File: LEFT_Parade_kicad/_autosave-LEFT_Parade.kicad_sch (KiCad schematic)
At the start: 31 parts, among them SW1 RotaryEncoder_Switch, SW10 SW_Push_reverse, SW11 SW_Push_reverse, SW12 SW_Push_reverse, SW13 SW_Push_reverse, SW14 SW_Push_reverse, SW15 SW_Push_reverse, SW16 SW_Push_reverse, SW17 SW_Push_reverse, SW2 SW_Push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

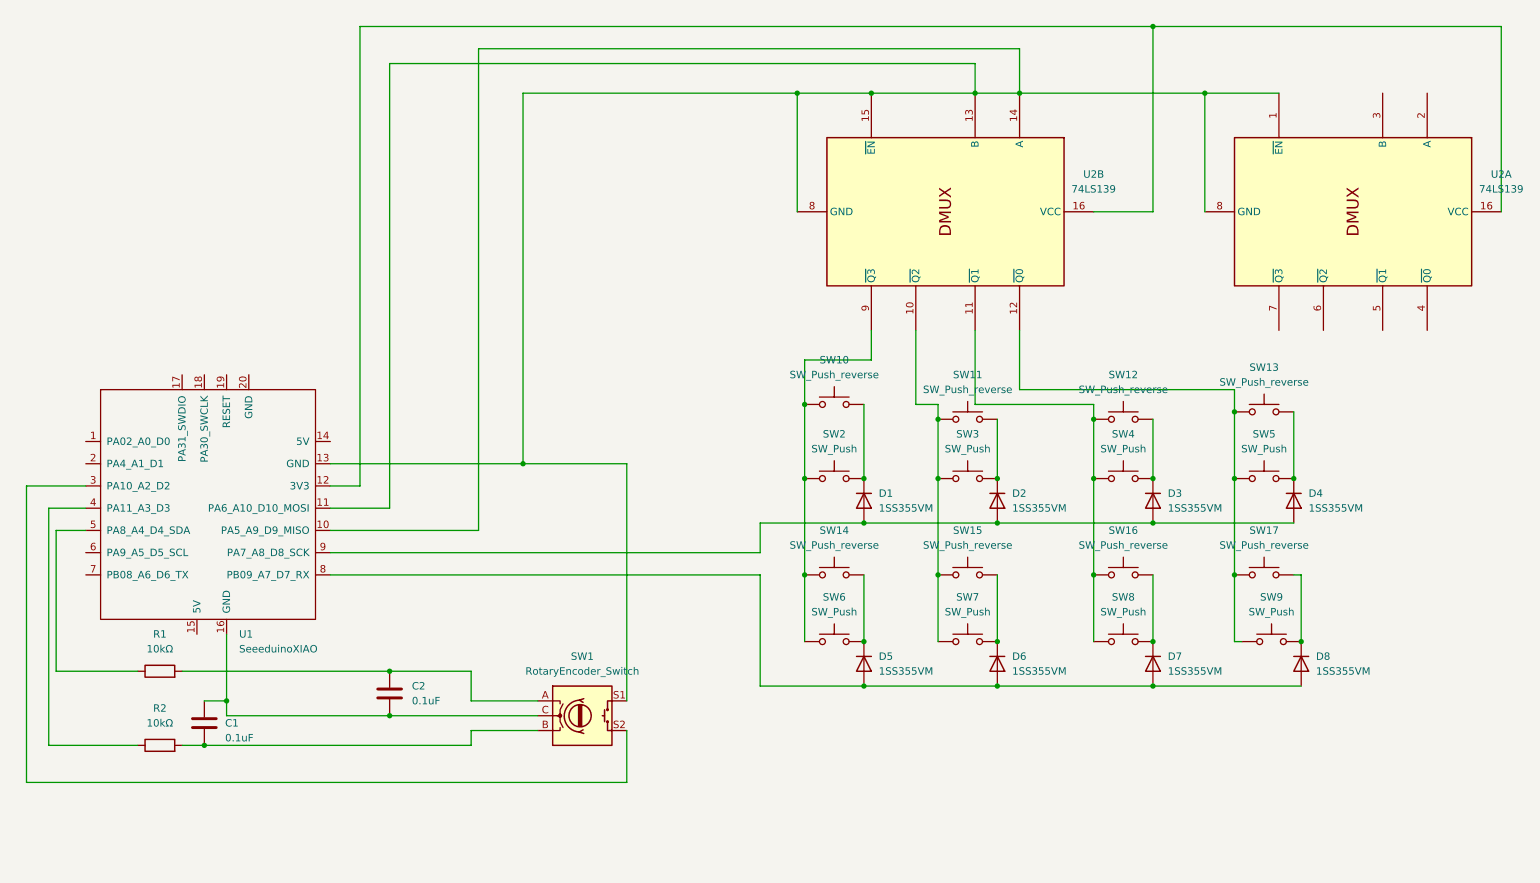
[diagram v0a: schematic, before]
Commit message: [modify] game mode operatin (turbo -> keep pushing)
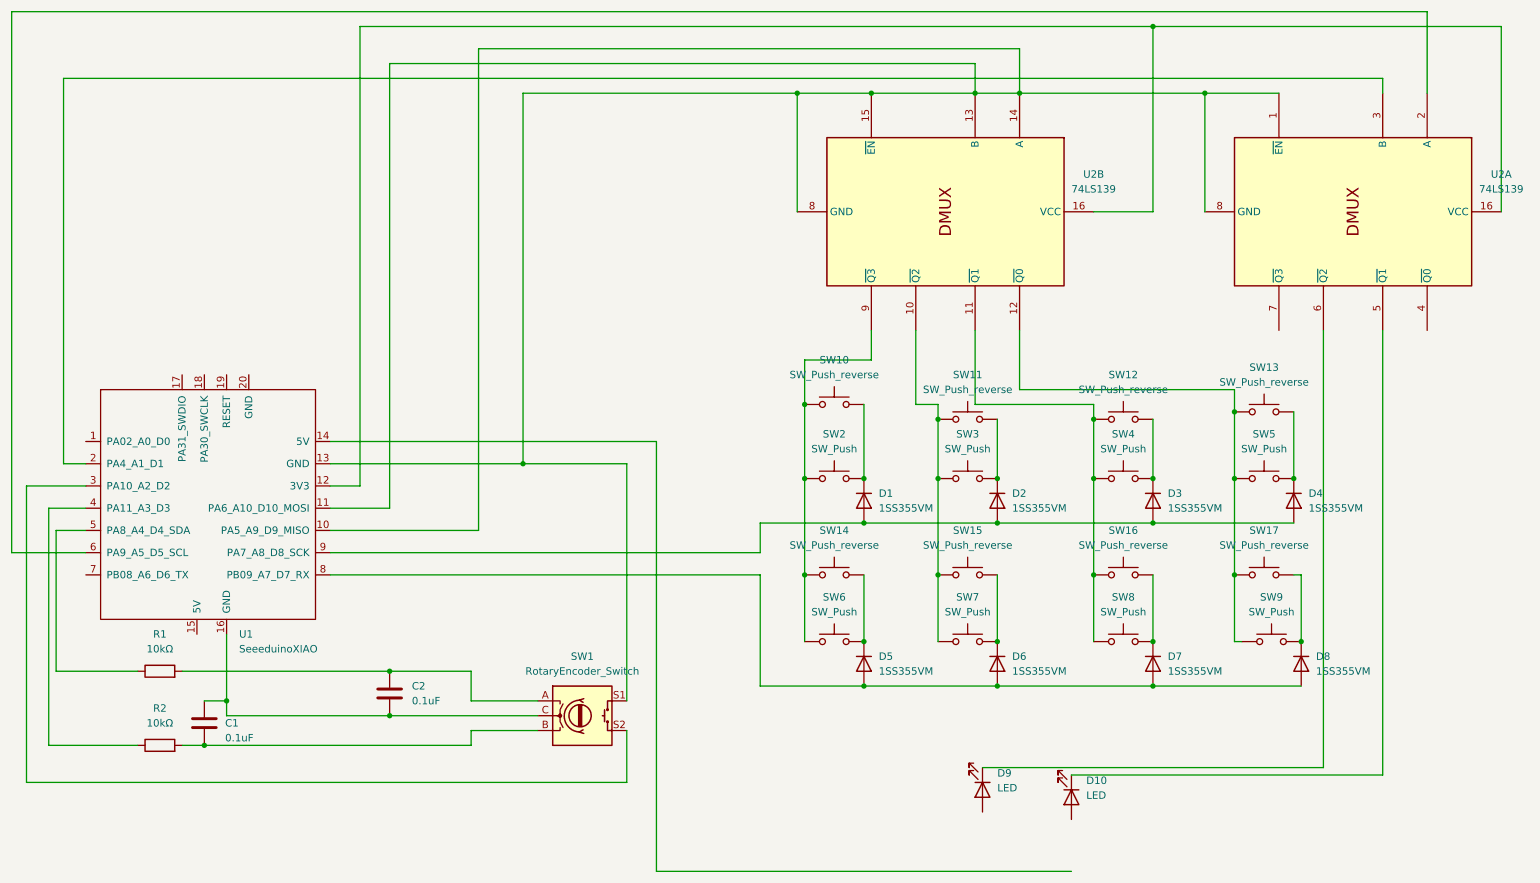
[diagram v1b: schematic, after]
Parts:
- added D10, D9: LED, symbol Device:LED
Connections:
- net at U2.2 (A): now also U1.6 (PA9_A5_D5_SCL)
- net at U2.3 (B): now also U1.2 (PA4_A1_D1)
- net at U2.5 (~{Q1}): now also D10.1 (K)
- net at U2.6 (~{Q2}): now also D9.1 (K)
